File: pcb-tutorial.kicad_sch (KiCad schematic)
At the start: 1 part, among them U1 ATmega32U4-A

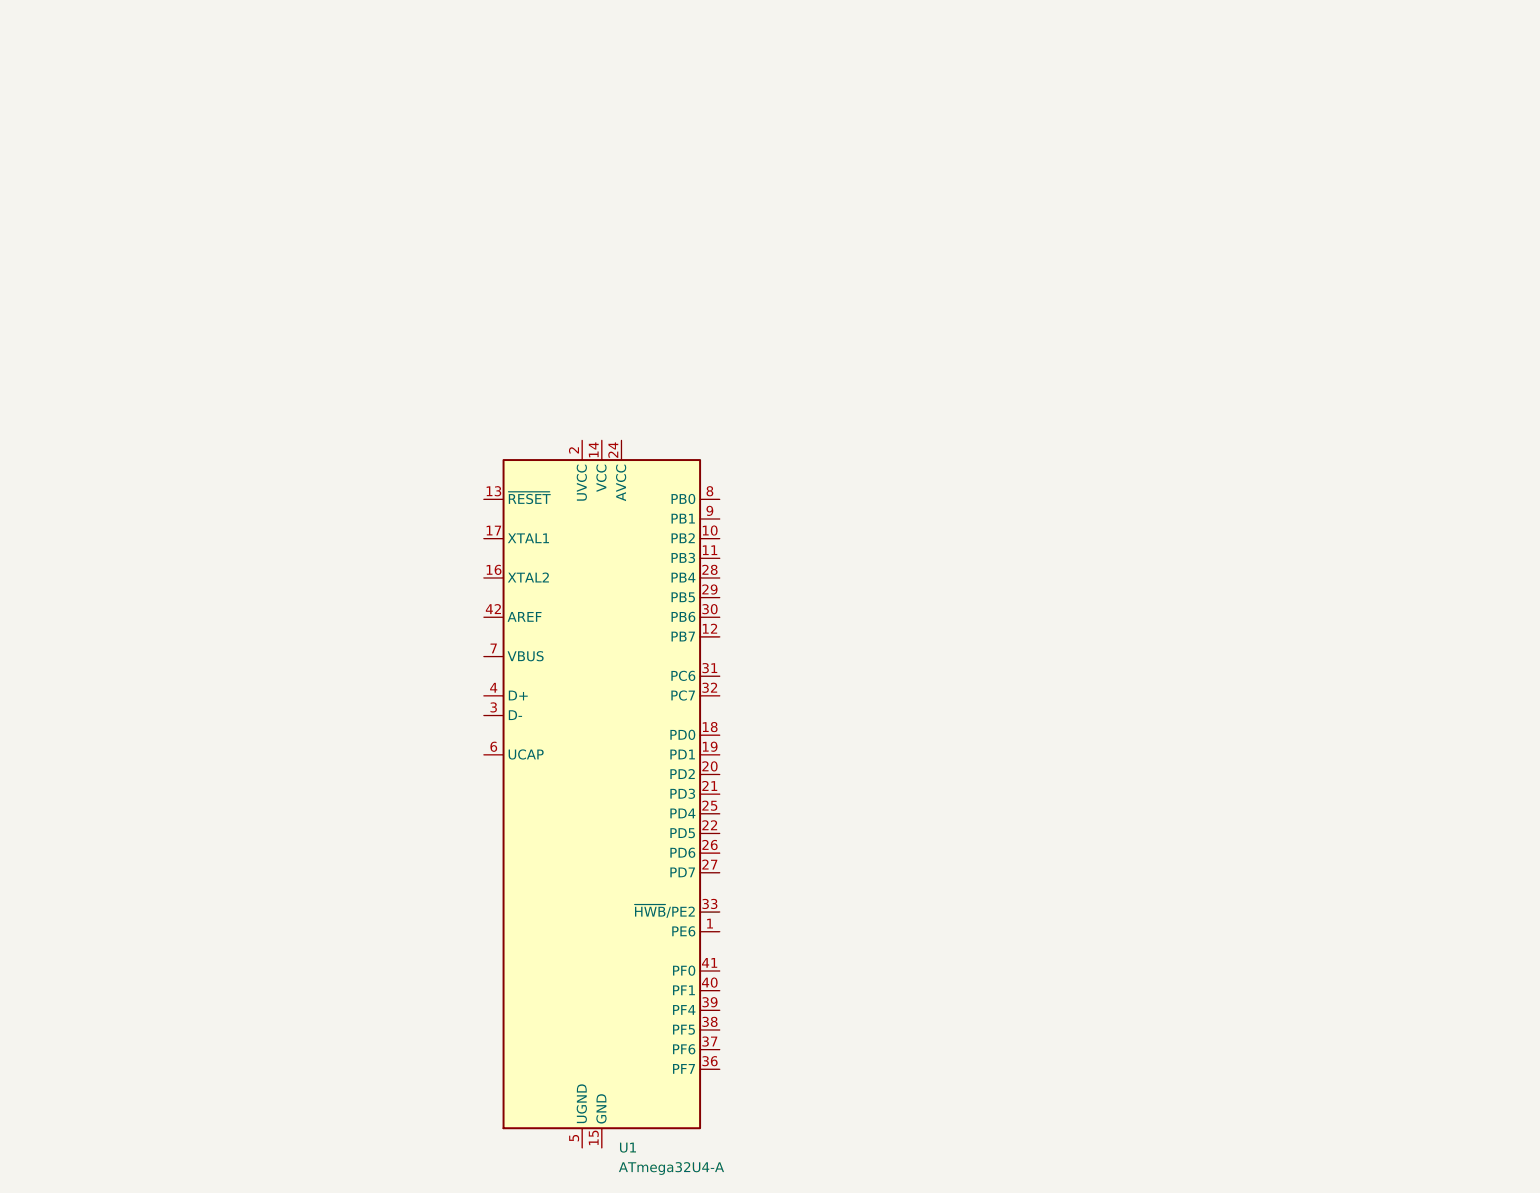
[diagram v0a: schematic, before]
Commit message: created mcu schematic
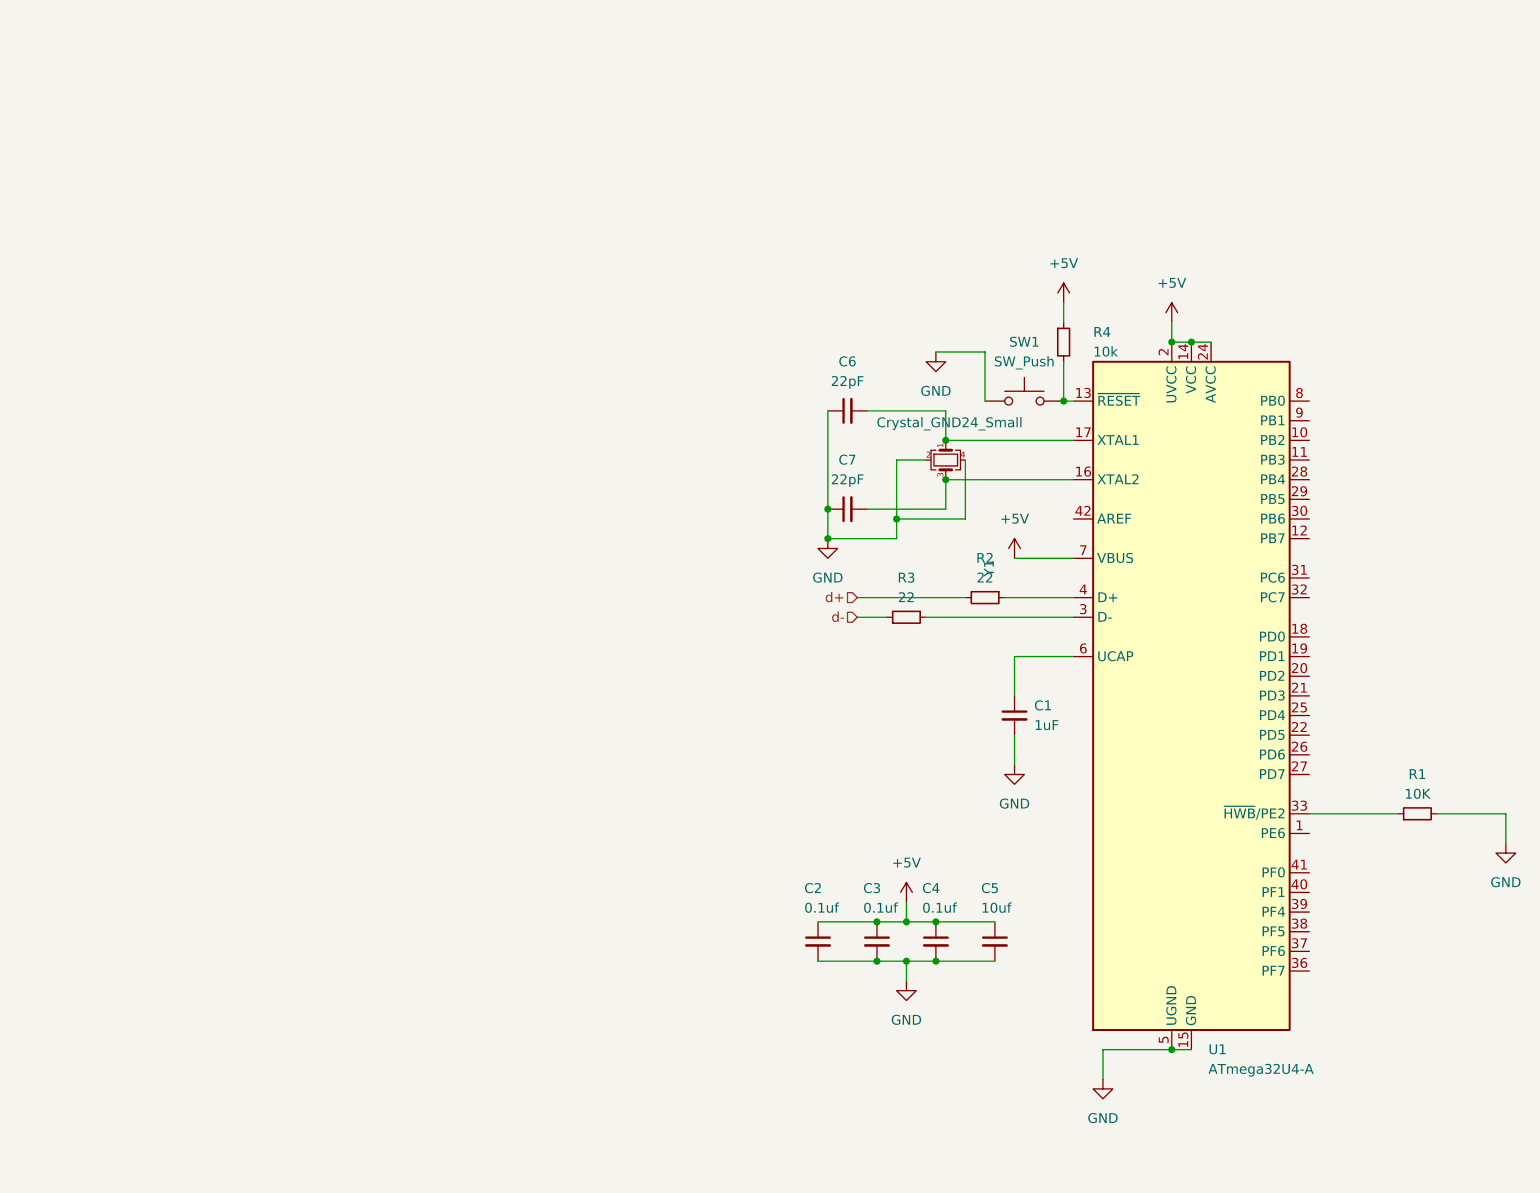
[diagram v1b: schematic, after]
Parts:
- added C1: 1uF, symbol Device:C_Small
- added C2, C3, C4: 0.1uf, symbol Device:C_Small
- added C5: 10uf, symbol Device:C_Small
- added C6, C7: 22pF, symbol Device:C_Small
- added R1: 10K, , symbol Device:R_Small
- added R2, R3: 22, symbol Device:R_Small
- added R4: 10k, symbol Device:R_Small
- added SW1: SW_Push, symbol Switch:SW_Push
- added Y1: Crystal_GND24_Small, symbol Device:Crystal_GND24_Small
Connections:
- net at U1.13 (~{RESET}): now also R4.2, SW1.2
- net +5V: now reaches U1.14 (VCC), U1.34 (VCC)
- net +5V: now also U1.2 (UVCC), U1.24 (AVCC), U1.44 (AVCC), U1.7 (VBUS), C2.1, C3.1, C4.1, C5.1, R4.1
- net GND: now reaches U1.15 (GND), U1.23 (GND), U1.35 (GND), U1.43 (GND)
- net GND: now also U1.5 (UGND), C1.2, C2.2, C3.2, C4.2, C5.2, C6.1, C7.1, R1.2, SW1.1, Y1.2, Y1.4
- net at U1.16 (XTAL2): now also C7.2, Y1.3
- net at U1.17 (XTAL1): now also C6.2, Y1.1
- net at U1.3 (D-): now also R3.2
- net at U1.33 (~{HWB}/PE2): now also R1.1
- net at U1.4 (D+): now also R2.1
- net at U1.6 (UCAP): now also C1.1
- new net d+: R2.2
- new net d-: R3.1
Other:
- moved on the sheet: U1

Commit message: full schematic
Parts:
- added D1, D2, D3, D4: D_Small, symbol Device:D_Small
- added F1: Polyfuse_Small, symbol Device:Polyfuse_Small
- added MX1, MX2, MX3, MX4: MX-NoLED, symbol MX_Alps_Hybrid:MX-NoLED
- added USB1: Molex-0548190589, symbol random-keyboard-parts:Molex-0548190589
- R1: footprint (none) -> (none)
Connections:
- net +5V: now also F1.2
- net GND: now also USB1.1 (GND)
- net d+: now also USB1.3 (D+)
- net d-: now also USB1.4 (D-)
- new net: D1.2 (A), MX1.2 (ROW)
- new net: D3.2 (A), MX3.2 (ROW)
- new net: D4.2 (A), MX4.2 (ROW)
- new net: D2.2 (A), MX2.2 (ROW)
- new net VCC: F1.1, USB1.5 (VBUS)
- new net col 0: MX1.1 (COL), MX3.1 (COL)
- new net col 1: MX2.1 (COL), MX4.1 (COL)
- new net row 0: D1.1 (K), D2.1 (K)
- new net row 1: D3.1 (K), D4.1 (K)

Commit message: almost done with pcb, need to route
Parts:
- C1, C2, C3, C4, C5, C6, C7: footprint (none) -> Capacitor_SMD:C_0805_2012Metric
- D1, D2, D3, D4: footprint (none) -> Diode_SMD:D_SOD-123
- F1: footprint (none) -> Fuse:Fuse_1206_3216Metric
- MX1, MX2, MX3, MX4: footprint (none) -> MX_Alps_Hybrid:MX-1U-NoLED
- R1, R2, R3, R4: footprint (none) -> Resistor_SMD:R_0805_2012Metric
- SW1: footprint (none) -> random-keyboard-parts:SKQG-1155865
- USB1: footprint (none) -> random-keyboard-parts:Molex-0548190589
- Y1: footprint (none) -> Crystal:Crystal_SMD_3225-4Pin_3.2x2.5mm
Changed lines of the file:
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@@
 			)
 		)
-		(property "Footprint" ""
+		(property "Footprint" "Diode_SMD:D_SOD-123"
 			(at 29.21 44.45 90)
 			(effects
@@
 			)
 		)
-		(property "Footprint" ""
+		(property "Footprint" "random-keyboard-parts:Molex-0548190589"
 			(at 168.91 33.02 0)
 			(effects
@@
 			)
 		)
-		(property "Footprint" ""
+		(property "Footprint" "Resistor_SMD:R_0805_2012Metric"
 			(at 149.86 59.69 0)
 			(effects
@@
 			)
 		)
-		(property "Footprint" ""
+		(property "Footprint" "Resistor_SMD:R_0805_2012Metric"
 			(at 195.58 120.65 0)
 			(effects
@@
 			)
 		)
-		(property "Footprint" ""
+		(property "Footprint" "MX_Alps_Hybrid:MX-1U-NoLED"
 			(at 18.415 62.865 0)
 			(effects
@@
 			)
 		)
-		(property "Footprint" ""
+		(property "Footprint" "Resistor_SMD:R_0805_2012Metric"
 			(at 139.7 92.71 0)
 			(effects
@@
 			)
 		)
-		(property "Footprint" ""
+		(property "Footprint" "Capacitor_SMD:C_0805_2012Metric"
 			(at 121.92 81.28 0)
 			(effects
@@
 			)
 		)
-		(property "Footprint" ""
+		(property "Footprint" "Capacitor_SMD:C_0805_2012Metric"
 			(at 125.73 137.16 0)
 			(effects
@@
 			)
 		)
-		(property "Footprint" ""
+		(property "Footprint" "Crystal:Crystal_SMD_3225-4Pin_3.2x2.5mm"
 			(at 134.62 74.93 0)
 			(effects
@@
 			)
 		)
-		(property "Footprint" ""
+		(property "Footprint" "Capacitor_SMD:C_0805_2012Metric"
 			(at 121.92 68.58 0)
 			(effects
@@
 			)
 		)
-		(property "Footprint" ""
+		(property "Footprint" "Diode_SMD:D_SOD-123"
 			(at 29.21 69.85 90)
 			(effects
@@
 			)
 		)
-		(property "Footprint" ""
+		(property "Footprint" "MX_Alps_Hybrid:MX-1U-NoLED"
 			(at 31.115 62.865 0)
 			(effects
@@
 			)
 		)
-		(property "Footprint" ""
+		(property "Footprint" "MX_Alps_Hybrid:MX-1U-NoLED"
 			(at 31.115 37.465 0)
 			(effects
@@
 			)
 		)
-		(property "Footprint" ""
+		(property "Footprint" "MX_Alps_Hybrid:MX-1U-NoLED"
 			(at 18.415 37.465 0)
 			(effects
@@
 			)
 		)
-		(property "Footprint" ""
+		(property "Footprint" "Capacitor_SMD:C_0805_2012Metric"
 			(at 140.97 137.16 0)
 			(effects
@@
 			)
 		)
-		(property "Footprint" ""
+		(property "Footprint" "random-keyboard-parts:SKQG-1155865"
 			(at 144.78 62.23 0)
 			(effects
@@
 			)
 		)
-		(property "Footprint" ""
+		(property "Footprint" "Capacitor_SMD:C_0805_2012Metric"
 			(at 118.11 137.16 0)
 			(effects
@@
 			)
 		)
-		(property "Footprint" ""
+		(property "Footprint" "Capacitor_SMD:C_0805_2012Metric"
 			(at 143.51 107.95 0)
 			(effects
@@
 			)
 		)
-		(property "Footprint" ""
+		(property "Footprint" "Diode_SMD:D_SOD-123"
 			(at 41.91 69.85 90)
 			(effects
@@
 			)
 		)
-		(property "Footprint" ""
+		(property "Footprint" "Fuse:Fuse_1206_3216Metric"
 			(at 194.31 26.67 0)
 			(effects
@@
 			)
 		)
-		(property "Footprint" ""
+		(property "Footprint" "Resistor_SMD:R_0805_2012Metric"
 			(at 129.54 95.25 0)
 			(effects
@@
 			)
 		)
-		(property "Footprint" ""
+		(property "Footprint" "Diode_SMD:D_SOD-123"
 			(at 41.91 44.45 90)
 			(effects
@@
 			)
 		)
-		(property "Footprint" ""
+		(property "Footprint" "Capacitor_SMD:C_0805_2012Metric"
 			(at 133.35 137.16 0)
 			(effects
